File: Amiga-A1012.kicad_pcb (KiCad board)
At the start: 2 copper layers, 10 parts, among them U1 74LS38, U2 74LS74, U3 74LS38

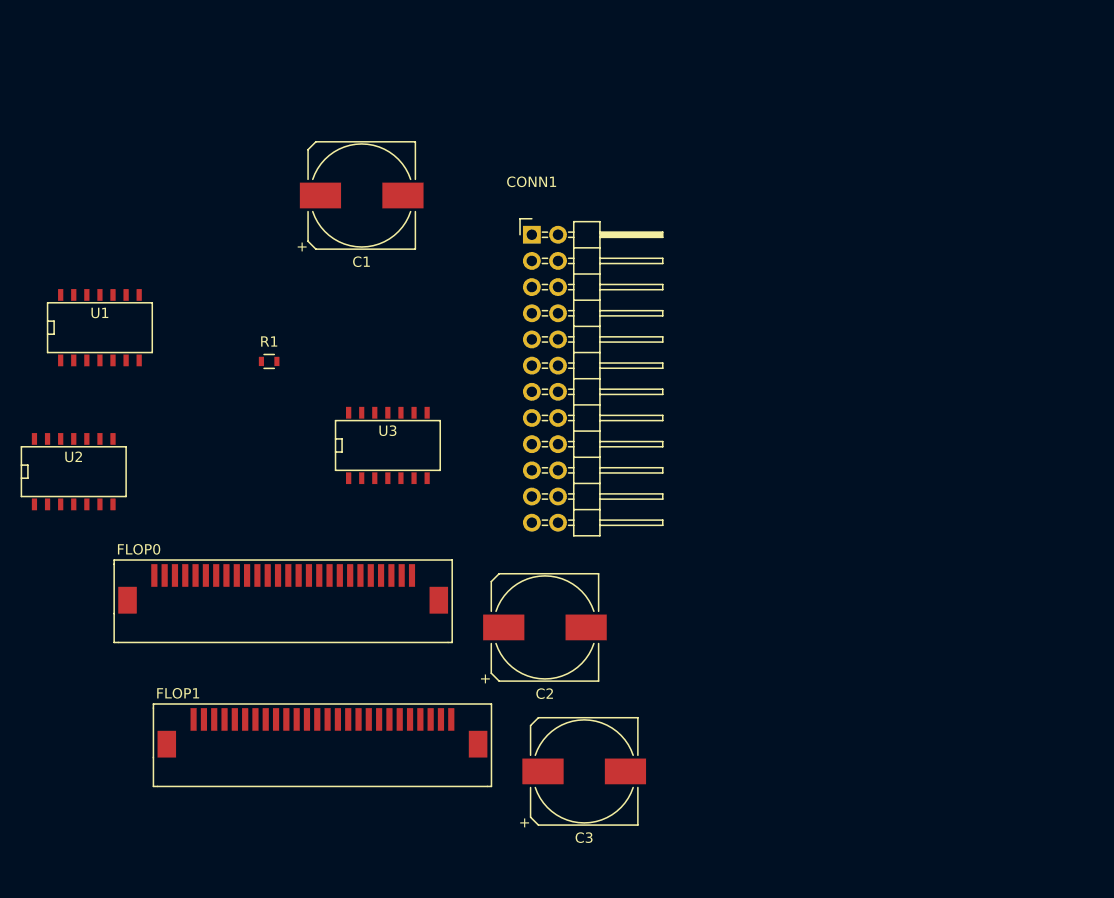
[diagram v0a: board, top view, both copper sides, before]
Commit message: Started placing and routing, only big caps and connectors.
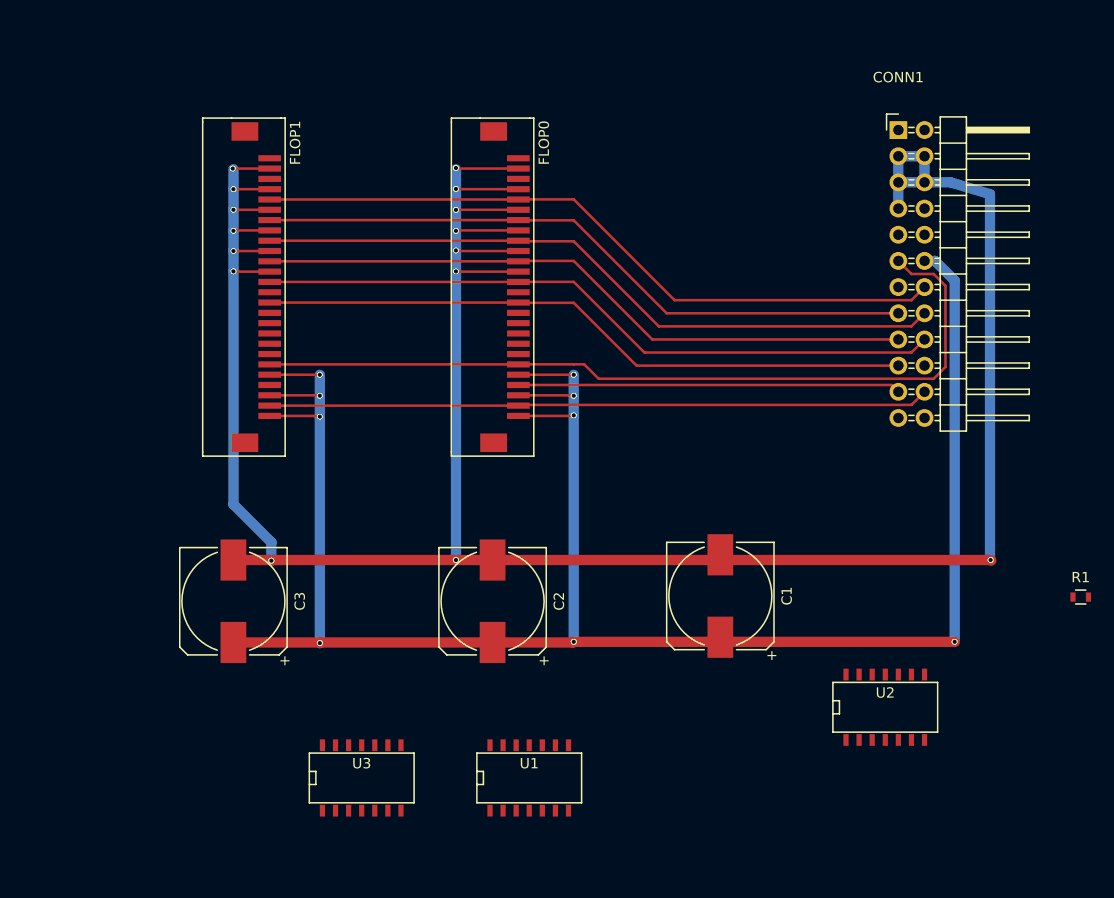
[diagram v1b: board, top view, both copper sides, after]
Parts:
- moved U2 82.0 mm to (208.3, 138.4)
- moved R1 82.0 mm to (227.2, 127.9)
- moved U1 60.4 mm to (173.7, 145.3)
- moved C1 52.2 mm to (192.3, 127.8), turned to 90 degrees
- moved FLOP1 45.1 mm to (146.1, 97.8), turned to 270 degrees
- moved C3 37.8 mm to (145.0, 128.3), turned to 90 degrees
- moved CONN1 37.0 mm to (209.6, 82.5)
- moved FLOP0 36.6 mm to (170.2, 97.8), turned to 270 degrees
- moved U3 32.4 mm to (157.5, 145.3)
- moved C2 5.68 mm to (170.2, 128.3), turned to 90 degrees
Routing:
- net GND: track 0.00 -> 263.4 mm, vias 0 -> 15
- net +5V: track 0.00 -> 190.7 mm, vias 0 -> 9
- net Net-(CONN1-Pad11): track 0.00 -> 80.1 mm
- net Net-(CONN1-Pad14): track 0.00 -> 68.1 mm
- net Net-(CONN1-Pad16): track 0.00 -> 67.5 mm
- net Net-(CONN1-Pad18): track 0.00 -> 66.9 mm
- net Net-(CONN1-Pad15): track 0.00 -> 64.7 mm
- net Net-(CONN1-Pad17): track 0.00 -> 64.2 mm
- net Net-(CONN1-Pad22): track 0.00 -> 64.1 mm
- net Net-(CONN1-Pad19): track 0.00 -> 63.5 mm
- net Net-(CONN1-Pad21): track 0.00 -> 37.1 mm

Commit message: Added decoupling caps. More routing.
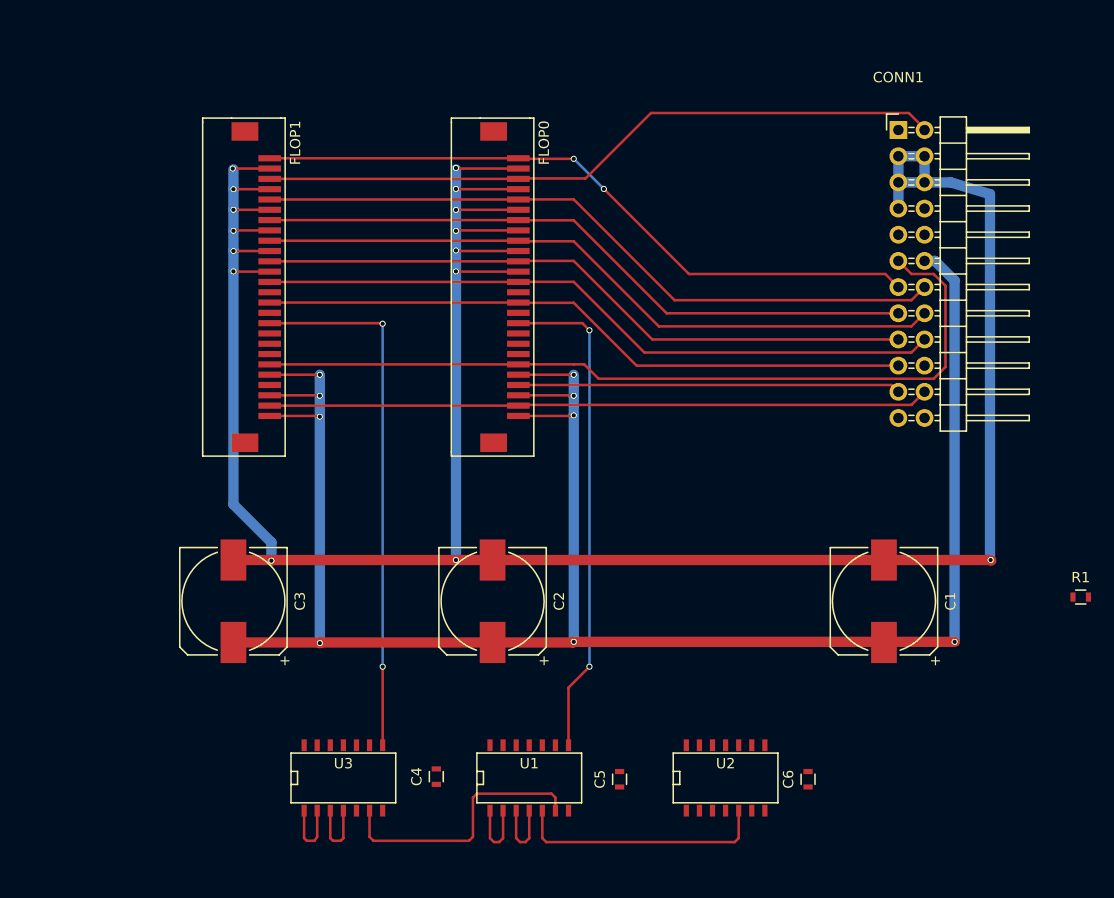
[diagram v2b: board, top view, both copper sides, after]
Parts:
- added C4: 100nF, Resistors_SMD:R_0603, F.Cu at (164.7, 145.3)
- added C5: 100nF, Resistors_SMD:R_0603, F.Cu at (182.5, 145.5)
- added C6: 100nF, Resistors_SMD:R_0603, F.Cu at (200.8, 145.5)
- moved U2 16.9 mm to (192.8, 145.3)
- moved C1 15.9 mm to (208.2, 128.3)
- moved U3 1.78 mm to (155.7, 145.3)
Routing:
- net Net-(CONN1-Pad2): track 0.00 -> 66.9 mm
- net Net-(CONN1-Pad13): track 0.00 -> 66.2 mm, vias 0 -> 2
- net Net-(FLOP1-Pad10): track 0.00 -> 51.9 mm, vias 0 -> 2
- net Net-(FLOP0-Pad10): track 0.00 -> 48.3 mm, vias 0 -> 2
- net Net-(CONN1-Pad1): track 0.00 -> 26.3 mm
- net Net-(U1-Pad5): track 0.00 -> 24.7 mm
- net Net-(CONN1-Pad21): track 37.1 -> 44.1 mm
- net Net-(U1-Pad3): track 0.00 -> 6.92 mm
- net Net-(U2-Pad12): track 0.00 -> 6.81 mm
- net Net-(CONN1-Pad9): track 0.00 -> 6.79 mm

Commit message: More routing. Connected VCC to +5V net, for LS chips.
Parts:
- moved R1 27.9 mm to (204.5, 144.0), turned to 90 degrees
- moved C4 0.25 mm to (164.7, 145.5), turned to 270 degrees
- turned C5 to 270 degrees
- turned C6 to 270 degrees
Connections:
- C4 pad 1: Net-(C4-Pad1) -> +5V
- C4 pad 2: Net-(C4-Pad2) -> GND
- C6 pad 1: Net-(C4-Pad1) -> +5V
- C6 pad 2: Net-(C4-Pad2) -> GND
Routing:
- net Net-(CONN1-Pad9): track 6.79 -> 138.8 mm, vias 0 -> 3
- net GND: track 263.4 -> 381.9 mm
- net Net-(CONN1-Pad1): track 26.3 -> 129.0 mm, vias 0 -> 2
- net +5V: track 190.7 -> 289.7 mm
- net Net-(CONN1-Pad8): track 0.00 -> 85.1 mm, vias 0 -> 4
- net Net-(U2-Pad9): track 0.00 -> 55.3 mm, vias 0 -> 2
- net Net-(U2-Pad12): track 6.81 -> 56.4 mm, vias 0 -> 2
- net Net-(U2-Pad8): track 0.00 -> 48.5 mm, vias 0 -> 2
- net Net-(CONN1-Pad21): track 44.1 -> 90.6 mm, vias 0 -> 2
- net Net-(U1-Pad10): track 0.00 -> 45.8 mm, vias 0 -> 2
- net Net-(R1-Pad2): track 0.00 -> 32.6 mm, vias 0 -> 2
- net Net-(U1-Pad3): track 6.92 -> 25.7 mm, vias 0 -> 2

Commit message: Finished routing. Fixed routing problems with unconnected nets. Added fiducials.
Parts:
- added REF**: Fiducial_1mm_Dia_2.54mm_Outer_CopperTop, Fiducials:Fiducial_1mm_Dia_2.54mm_Outer_CopperTop, F.Cu at (139.8, 151.8)
- added REF**: Fiducial_1mm_Dia_2.54mm_Outer_CopperTop, Fiducials:Fiducial_1mm_Dia_2.54mm_Outer_CopperTop, F.Cu at (139.8, 78.1)
- added REF**: Fiducial_1mm_Dia_2.54mm_Outer_CopperTop, Fiducials:Fiducial_1mm_Dia_2.54mm_Outer_CopperTop, F.Cu at (221.5, 151.8)
- moved C2 0.13 mm to (170.3, 128.3)
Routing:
- net Net-(R1-Pad2): track 32.6 -> 42.0 mm, vias 2 -> 4
- net GND: track 381.9 -> 389.2 mm
- net +5V: track 289.7 -> 292.6 mm
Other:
- board outline added: 88 x 80 mm

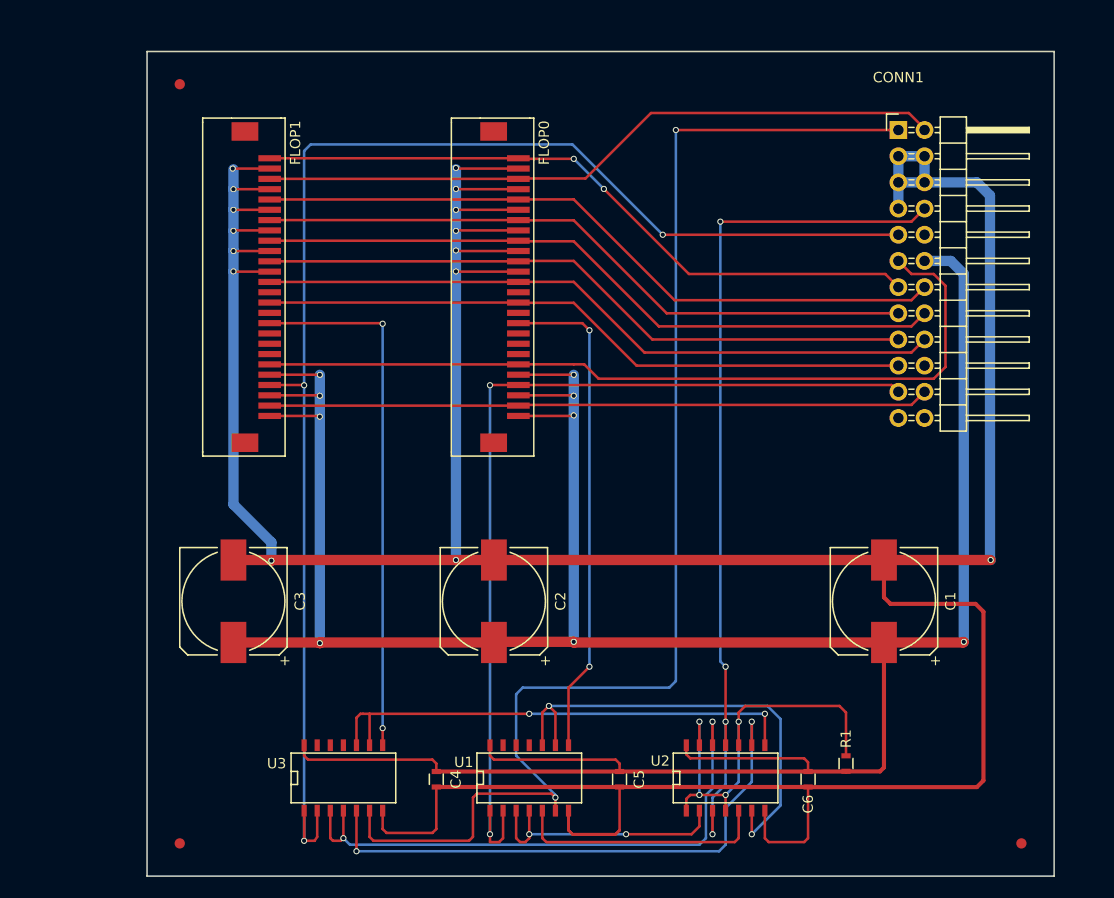
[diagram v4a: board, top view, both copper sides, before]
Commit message: Added mounting holes, moved fiducials.
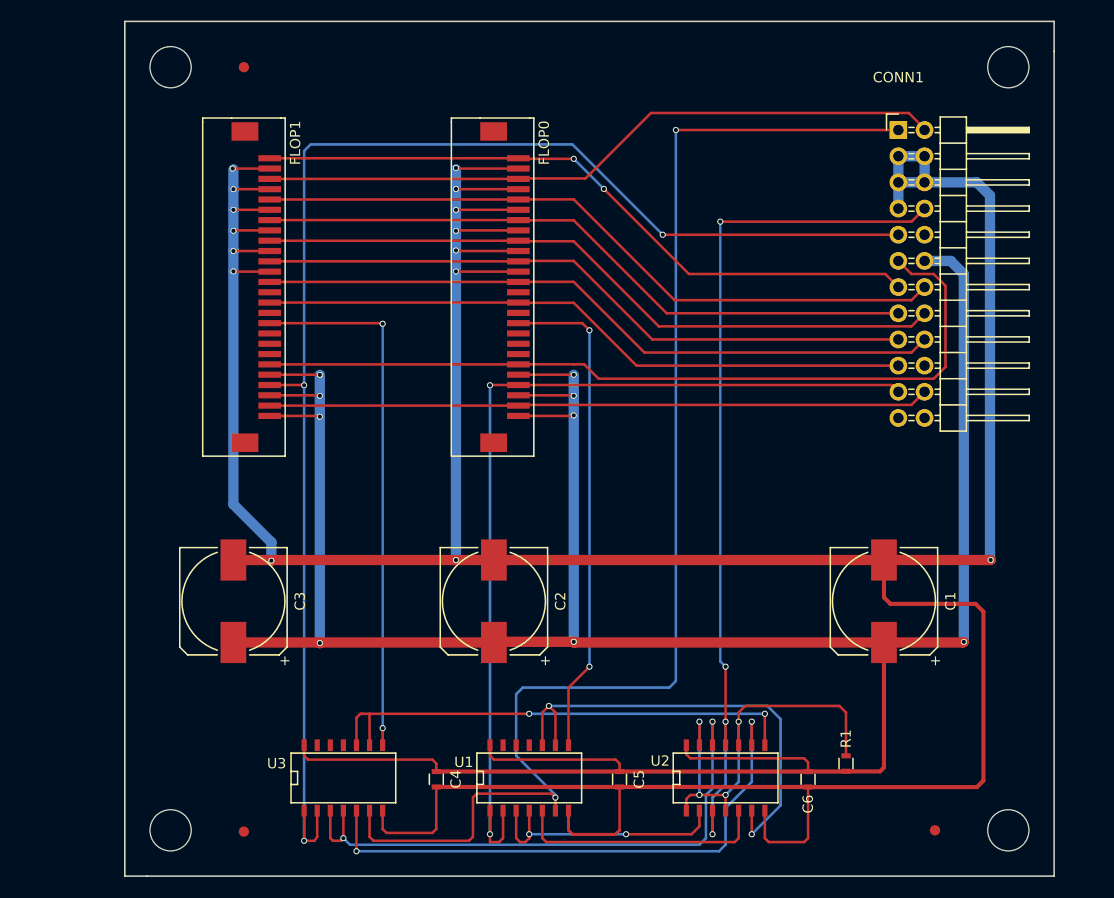
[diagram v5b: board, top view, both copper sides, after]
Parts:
- added REF**: MountingHole_4mm, Mounting_Holes:MountingHole_4mm, F.Cu at (138.9, 76.5)
- added REF**: MountingHole_4mm, Mounting_Holes:MountingHole_4mm, F.Cu at (138.9, 150.5)
- added REF**: MountingHole_4mm, Mounting_Holes:MountingHole_4mm, F.Cu at (220.2, 150.5)
- added REF**: MountingHole_4mm, Mounting_Holes:MountingHole_4mm, F.Cu at (220.2, 76.5)
- moved REF** 8.48 mm to (213.1, 150.5)
- moved REF** 6.44 mm to (146.1, 76.5)
- moved REF** 6.33 mm to (146.1, 150.6)
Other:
- board size 88 x 80 mm -> 90.2 x 82.9 mm
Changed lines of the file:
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@@
     (links 87)
     (no_connects 0)
-    (area 0 0 0 0)
+    (area 129.111904 67.507 234.973 156.57)
     (thickness 1.6)
-    (drawings 6)
+    (drawings 8)
     (tracks 399)
     (zones 0)
-    (modules 16)
+    (modules 20)
     (nets 39)
   )
@@
   )
   (setup
-    (last_trace_width 1)
+    (last_trace_width 0.25)
     (user_trace_width 0.4)
     (user_trace_width 1)
@@
     (pad_drill 0.762)
     (pad_to_mask_clearance 0.2)
-    (aux_axis_origin 136.652 154.94)
+    (aux_axis_origin 134.493 154.94)
     (visible_elements FFFFFF7F)
     (pcbplotparams
@@
       (outputformat 1)
       (mirror false)
-      (drillshape 1)
+      (drillshape 0)
       (scaleselection 1)
       (outputdirectory ""))
@@
   )
   (module Fiducials:Fiducial_1mm_Dia_2.54mm_Outer_CopperTop (layer F.Cu)
-    (at 139.827 151.765)
+    (at 146.05 150.622)
     (descr "Circular Fiducial, 1mm bare copper top; 2.54mm keepout")
     (tags marker)
@@
   )
   (module Fiducials:Fiducial_1mm_Dia_2.54mm_Outer_CopperTop (layer F.Cu)
-    (at 139.827 78.105)
+    (at 146.05 76.454)
     (descr "Circular Fiducial, 1mm bare copper top; 2.54mm keepout")
     (tags marker)
@@
   )
   (module Fiducials:Fiducial_1mm_Dia_2.54mm_Outer_CopperTop (layer F.Cu)
-    (at 221.488 151.765)
+    (at 213.106 150.495)
     (descr "Circular Fiducial, 1mm bare copper top; 2.54mm keepout")
     (tags marker)
@@
       (solder_mask_margin 0.77) (clearance 0.77))
   )
-  (dimension 80.01 (width 0.3) (layer F.Fab)
-    (gr_text "80.010 mm" (at 228.727 114.935 270) (layer F.Fab)
+  (module Mounting_Holes:MountingHole_4mm (layer F.Cu)
+    (at 138.938 76.454)
+    (descr "Mounting Hole 4mm, no annular")
+    (tags "mounting hole 4mm no annular")
+    (fp_text reference REF** (at 0 -5) (layer F.SilkS) hide
+      (effects (font (size 1 1) (thickness 0.15)))
+    )
+    (fp_text value MountingHole_4mm (at 0 5) (layer F.Fab) hide
+      (effects (font (size 1 1) (thickness 0.15)))
+    )
+    (fp_circle (center 0 0) (end 4 0) (layer Cmts.User) (width 0.15))
+    (fp_circle (center 0 0) (end 4.25 0) (layer F.CrtYd) (width 0.05))
+    (pad 1 np_thru_hole circle (at 0 0) (size 4 4) (drill 4) (layers *.Cu *.Mask))
+  )
+  (module Mounting_Holes:MountingHole_4mm (layer F.Cu)
+    (at 138.938 150.495)
+    (descr "Mounting Hole 4mm, no annular")
+    (tags "mounting hole 4mm no annular")
+    (fp_text reference REF** (at 0 -5) (layer F.SilkS) hide
+      (effects (font (size 1 1) (thickness 0.15)))
+    )
+    (fp_text value MountingHole_4mm (at 0 5) (layer F.Fab) hide
+      (effects (font (size 1 1) (thickness 0.15)))
+    )
+    (fp_circle (center 0 0) (end 4 0) (layer Cmts.User) (width 0.15))
+    (fp_circle (center 0 0) (end 4.25 0) (layer F.CrtYd) (width 0.05))
+    (pad 1 np_thru_hole circle (at 0 0) (size 4 4) (drill 4) (layers *.Cu *.Mask))
+  )
+  (module Mounting_Holes:MountingHole_4mm (layer F.Cu)
+    (at 220.218 150.495)
+    (descr "Mounting Hole 4mm, no annular")
+    (tags "mounting hole 4mm no annular")
+    (fp_text reference REF** (at 0 -5) (layer F.SilkS) hide
+      (effects (font (size 1 1) (thickness 0.15)))
+    )
+    (fp_text value MountingHole_4mm (at 0 5) (layer F.Fab) hide
+      (effects (font (size 1 1) (thickness 0.15)))
+    )
+    (fp_circle (center 0 0) (end 4 0) (layer Cmts.User) (width 0.15))
+    (fp_circle (center 0 0) (end 4.25 0) (layer F.CrtYd) (width 0.05))
+    (pad 1 np_thru_hole circle (at 0 0) (size 4 4) (drill 4) (layers *.Cu *.Mask))
+  )
+  (module Mounting_Holes:MountingHole_4mm (layer F.Cu)
+    (at 220.218 76.454)
+    (descr "Mounting Hole 4mm, no annular")
+    (tags "mounting hole 4mm no annular")
+    (fp_text reference REF** (at 0 -5) (layer F.SilkS) hide
+      (effects (font (size 1 1) (thickness 0.15)))
+    )
+    (fp_text value MountingHole_4mm (at 0 5) (layer F.Fab) hide
+      (effects (font (size 1 1) (thickness 0.15)))
+    )
+    (fp_circle (center 0 0) (end 4 0) (layer Cmts.User) (width 0.15))
+    (fp_circle (center 0 0) (end 4.25 0) (layer F.CrtYd) (width 0.05))
+    (pad 1 np_thru_hole circle (at 0 0) (size 4 4) (drill 4) (layers *.Cu *.Mask))
+  )
+  (dimension 90.17 (width 0.3) (layer F.Fab)
+    (gr_text "90.170 mm" (at 179.578 68.707) (layer F.Fab)
       (effects (font (size 1.5 1.5) (thickness 0.3)))
     )
-    (feature1 (pts (xy 227.203 154.94) (xy 227.203 154.94)))
-    (feature2 (pts (xy 227.203 74.93) (xy 227.203 74.93)))
-    (crossbar (pts (xy 227.203 74.93) (xy 227.203 154.94)))
-    (arrow1a (pts (xy 227.203 154.94) (xy 226.616579 153.813496)))
-    (arrow1b (pts (xy 227.203 154.94) (xy 227.789421 153.813496)))
-    (arrow2a (pts (xy 227.203 74.93) (xy 226.616579 76.056504)))
-    (arrow2b (pts (xy 227.203 74.93) (xy 227.789421 76.056504)))
-  )
-  (dimension 88.011 (width 0.3) (layer F.Fab)
-    (gr_text "88.011 mm" (at 180.721 70.866) (layer F.Fab)
+    (feature1 (pts (xy 134.493 70.739) (xy 134.493 70.739)))
+    (feature2 (pts (xy 224.663 70.739) (xy 224.663 70.739)))
+    (crossbar (pts (xy 224.663 70.739) (xy 134.493 70.739)))
+    (arrow1a (pts (xy 134.493 70.739) (xy 135.619504 70.152579)))
+    (arrow1b (pts (xy 134.493 70.739) (xy 135.619504 71.325421)))
+    (arrow2a (pts (xy 224.663 70.739) (xy 223.536496 70.152579)))
+    (arrow2b (pts (xy 224.663 70.739) (xy 223.536496 71.325421)))
+  )
+  (dimension 82.931097 (width 0.3) (layer F.Fab)
+    (gr_text "82.931 mm" (at 228.473 113.665 89.91225768) (layer F.Fab)
       (effects (font (size 1.5 1.5) (thickness 0.3)))
     )
-    (feature1 (pts (xy 224.663 72.39) (xy 224.663 72.39)))
-    (feature2 (pts (xy 136.652 72.39) (xy 136.652 72.39)))
-    (crossbar (pts (xy 136.652 72.39) (xy 224.663 72.39)))
-    (arrow1a (pts (xy 224.663 72.39) (xy 223.536496 72.976421)))
-    (arrow1b (pts (xy 224.663 72.39) (xy 223.536496 71.803579)))
-    (arrow2a (pts (xy 136.652 72.39) (xy 137.778504 72.976421)))
-    (arrow2b (pts (xy 136.652 72.39) (xy 137.778504 71.803579)))
-  )
+    (feature1 (pts (xy 225.806 154.94) (xy 225.806 154.94)))
+    (feature2 (pts (xy 225.933 72.009) (xy 225.933 72.009)))
+    (crossbar (pts (xy 225.933 72.009) (xy 225.806 154.94)))
+    (arrow1a (pts (xy 225.806 154.94) (xy 225.221305 153.8126)))
+    (arrow1b (pts (xy 225.806 154.94) (xy 226.394145 153.814396)))
+    (arrow2a (pts (xy 225.933 72.009) (xy 225.344855 73.134604)))
+    (arrow2b (pts (xy 225.933 72.009) (xy 226.517695 73.1364)))
+  )
+  (gr_line (start 134.493 154.94) (end 136.652 154.94) (angle 90) (layer Edge.Cuts) (width 0.15))
+  (gr_line (start 134.493 72.009) (end 134.493 154.94) (angle 90) (layer Edge.Cuts) (width 0.15))
+  (gr_line (start 224.663 72.009) (end 134.493 72.009) (angle 90) (layer Edge.Cuts) (width 0.15))
+  (gr_line (start 224.663 74.93) (end 224.663 72.009) (angle 90) (layer Edge.Cuts) (width 0.15))
   (gr_line (start 224.663 154.94) (end 224.663 74.93) (angle 90) (layer Edge.Cuts) (width 0.15))
   (gr_line (start 136.652 154.94) (end 224.663 154.94) (angle 90) (layer Edge.Cuts) (width 0.15))
-  (gr_line (start 136.652 74.93) (end 136.652 154.94) (angle 90) (layer Edge.Cuts) (width 0.15))
-  (gr_line (start 224.663 74.93) (end 136.652 74.93) (angle 90) (layer Edge.Cuts) (width 0.15))
   (segment (start 212.09 95.25) (end 214.63 95.25) (width 1) (layer B.Cu) (net 1))
   (segment (start 215.837 132.27) (end 208.153 132.27) (width 1) (layer F.Cu) (net 1))
